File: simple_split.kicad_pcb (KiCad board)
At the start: 2 copper layers, 182.1 x 114.5 mm, 103 parts, among them J1 AudioJack3, J2 Conn_01x02, M1 MountingHole, M2 MountingHole, M3 MountingHole, M4 MountingHole, M5 MountingHole, M6 MountingHole, M7 MountingHole, M8 MountingHole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

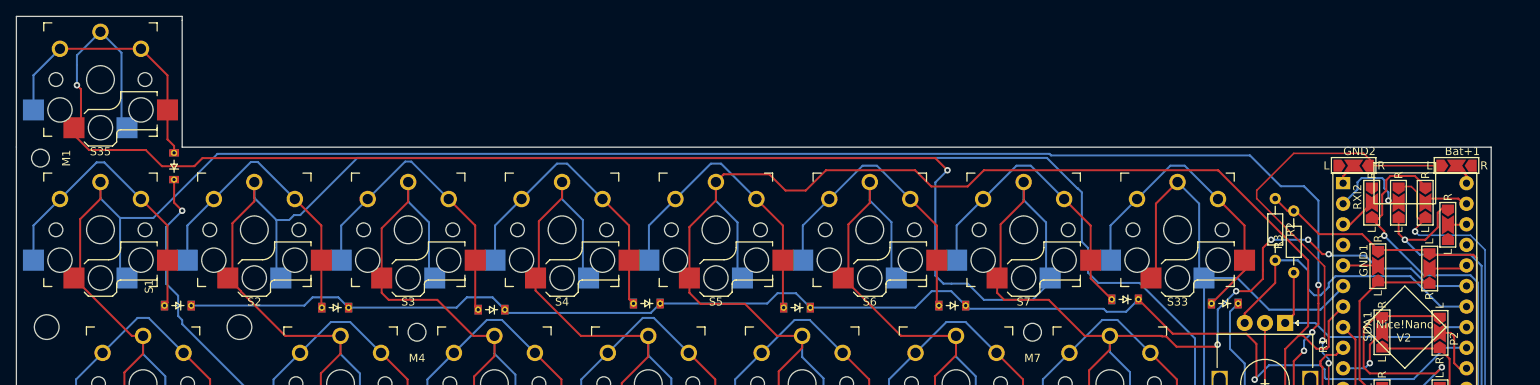
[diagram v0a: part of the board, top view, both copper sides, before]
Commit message: added 7 keys
14 in total between two sides
-F1-12
-2 multipurpose
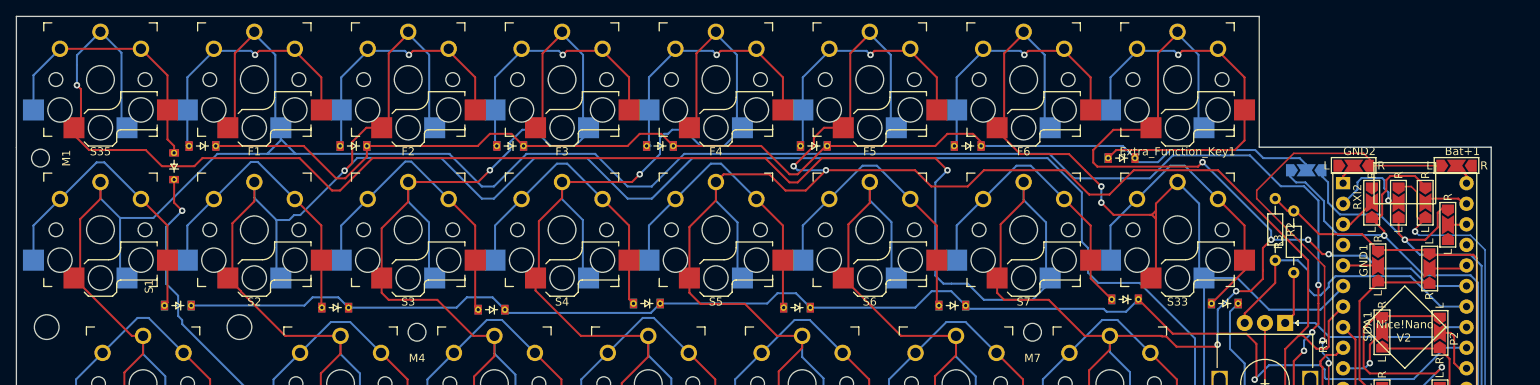
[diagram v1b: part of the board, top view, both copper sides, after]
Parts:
- added D34: D, Misc Keyboard Parts:reversable_diode, F.Cu at (132.5, 99.0)
- added D36: D, Misc Keyboard Parts:reversable_diode, F.Cu at (151.2, 99.0)
- added D37: D, Misc Keyboard Parts:reversable_diode, F.Cu at (170.5, 99.0)
- added D38: D, Misc Keyboard Parts:reversable_diode, F.Cu at (189.0, 99.0)
- added D39: D, Misc Keyboard Parts:reversable_diode, F.Cu at (208.0, 99.0)
- added D40: D, Misc Keyboard Parts:reversable_diode, F.Cu at (227.0, 99.0)
- added D41: D, Misc Keyboard Parts:reversable_diode, F.Cu at (246.0, 100.5)
- added ExtraButtonsSelect1: ~, Misc Keyboard Parts:Side Indicator - Improved, B.Cu at (268.8, 102.0)
- added Extra_Function_Key1: ~, keyswitches:Kailh_socket_PG1350_optional_reversible, F.Cu at (252.9, 90.8)
- added F1: ~, keyswitches:Kailh_socket_PG1350_optional_reversible, F.Cu at (138.9, 90.8)
- added F2: ~, keyswitches:Kailh_socket_PG1350_optional_reversible, F.Cu at (157.9, 90.8)
- added F3: ~, keyswitches:Kailh_socket_PG1350_optional_reversible, F.Cu at (176.9, 90.8)
- added F4: ~, keyswitches:Kailh_socket_PG1350_optional_reversible, F.Cu at (195.9, 90.8)
- added F5: ~, keyswitches:Kailh_socket_PG1350_optional_reversible, F.Cu at (214.9, 90.8)
- added F6: ~, keyswitches:Kailh_socket_PG1350_optional_reversible, F.Cu at (233.9, 90.8)
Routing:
- net /6: track 0.00 -> 147.6 mm
- net /G: track 383.8 -> 452.8 mm, vias 7 -> 8
- net /D: track 322.4 -> 374.6 mm, vias 1 -> 2
- net /C: track 366.0 -> 417.9 mm, vias 2 -> 3
- net /F: track 253.4 -> 304.0 mm, vias 0 -> 2
- net Net-(D41-A): track 0.00 -> 49.8 mm, vias 0 -> 1
- net /A: track 367.4 -> 408.7 mm
- net /B: track 348.4 -> 389.3 mm, vias 3 -> 4
- net /E: track 273.3 -> 312.9 mm, vias 0 -> 2
- net Net-(D38-A): track 0.00 -> 32.8 mm, vias 0 -> 1
- net Net-(D37-A): track 0.00 -> 32.8 mm, vias 0 -> 1
- net Net-(D34-A): track 0.00 -> 32.8 mm, vias 0 -> 1
- net Net-(D36-A): track 0.00 -> 32.7 mm, vias 0 -> 1
- net Net-(D40-A): track 0.00 -> 32.5 mm, vias 0 -> 1
- net Net-(D39-A): track 0.00 -> 32.5 mm, vias 0 -> 1
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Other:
- outline, holes or cut-outs redrawn

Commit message: Finished V6
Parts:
- added M10: MountingHole, MountingHole:MountingHole_2.2mm_M2, F.Cu at (243.5, 87.5)
- added M11: MountingHole, MountingHole:MountingHole_2.2mm_M2, F.Cu at (186.5, 87.0)
- moved D36 4.18 mm to (147.0, 99.5), turned to 90 degrees
- moved D34 3.91 mm to (130.0, 102.0), turned to 90 degrees
- moved D37 2.50 mm to (168.5, 100.5)
- moved D40 2.24 mm to (228.0, 101.0)
- moved D39 2.12 mm to (206.5, 100.5)
- moved D38 1.89 mm to (187.8, 100.5)
- moved D35 1.00 mm to (128.0, 101.5)
- moved D41 0.50 mm to (246.0, 101.0)
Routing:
- net /6: track 147.6 -> 160.2 mm, vias 0 -> 1
- net /B: track 389.3 -> 394.7 mm
- net /A: track 408.7 -> 413.7 mm
- net Net-(D40-A): track 32.5 -> 35.0 mm
- net Net-(D39-A): track 32.5 -> 34.9 mm
- net Net-(D37-A): track 32.8 -> 34.9 mm
- net Net-(D38-A): track 32.8 -> 34.8 mm
- net /G: track 452.8 -> 454.4 mm
- net Net-(D34-A): track 32.8 -> 34.3 mm
- net /C: track 417.9 -> 419.0 mm
- net /E: track 312.9 -> 312.3 mm
